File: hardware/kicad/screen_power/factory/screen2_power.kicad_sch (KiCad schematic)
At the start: 18 parts, among them J203 SCREEN POWER 5V 3A, Q201 2N7002, Q202 2N7002, U202 SN74LVC1G14DBVR, U203 TPS25221DBVR, U204 TPS25810RVCR

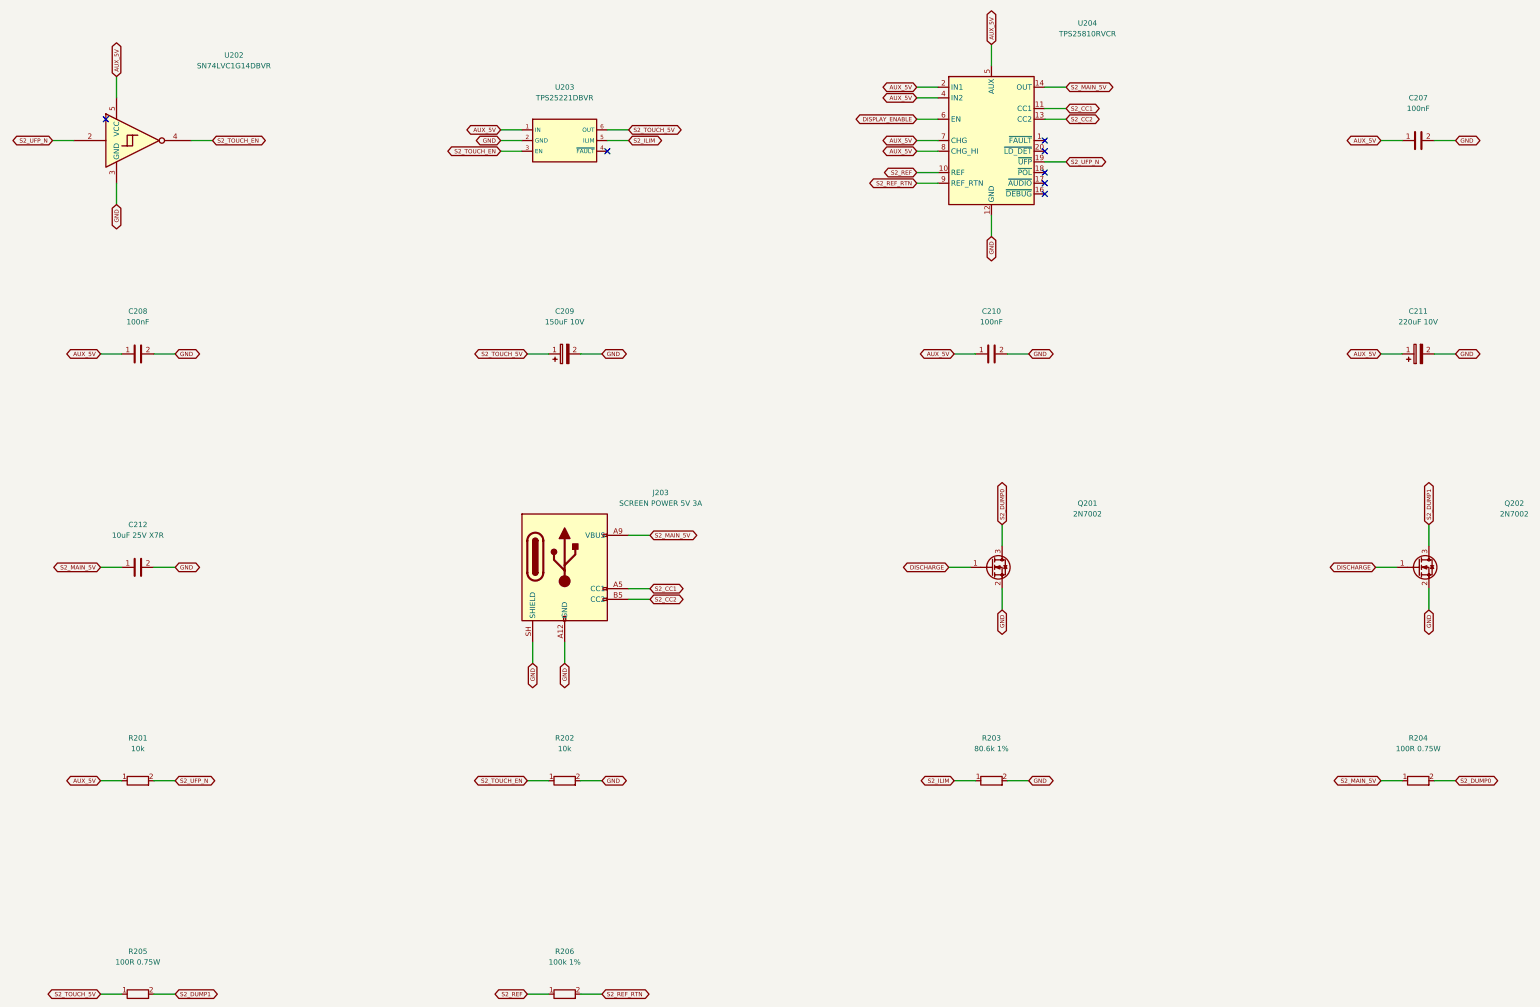
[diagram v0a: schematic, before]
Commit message: refactor(hardware): simplify and compact screen power boards
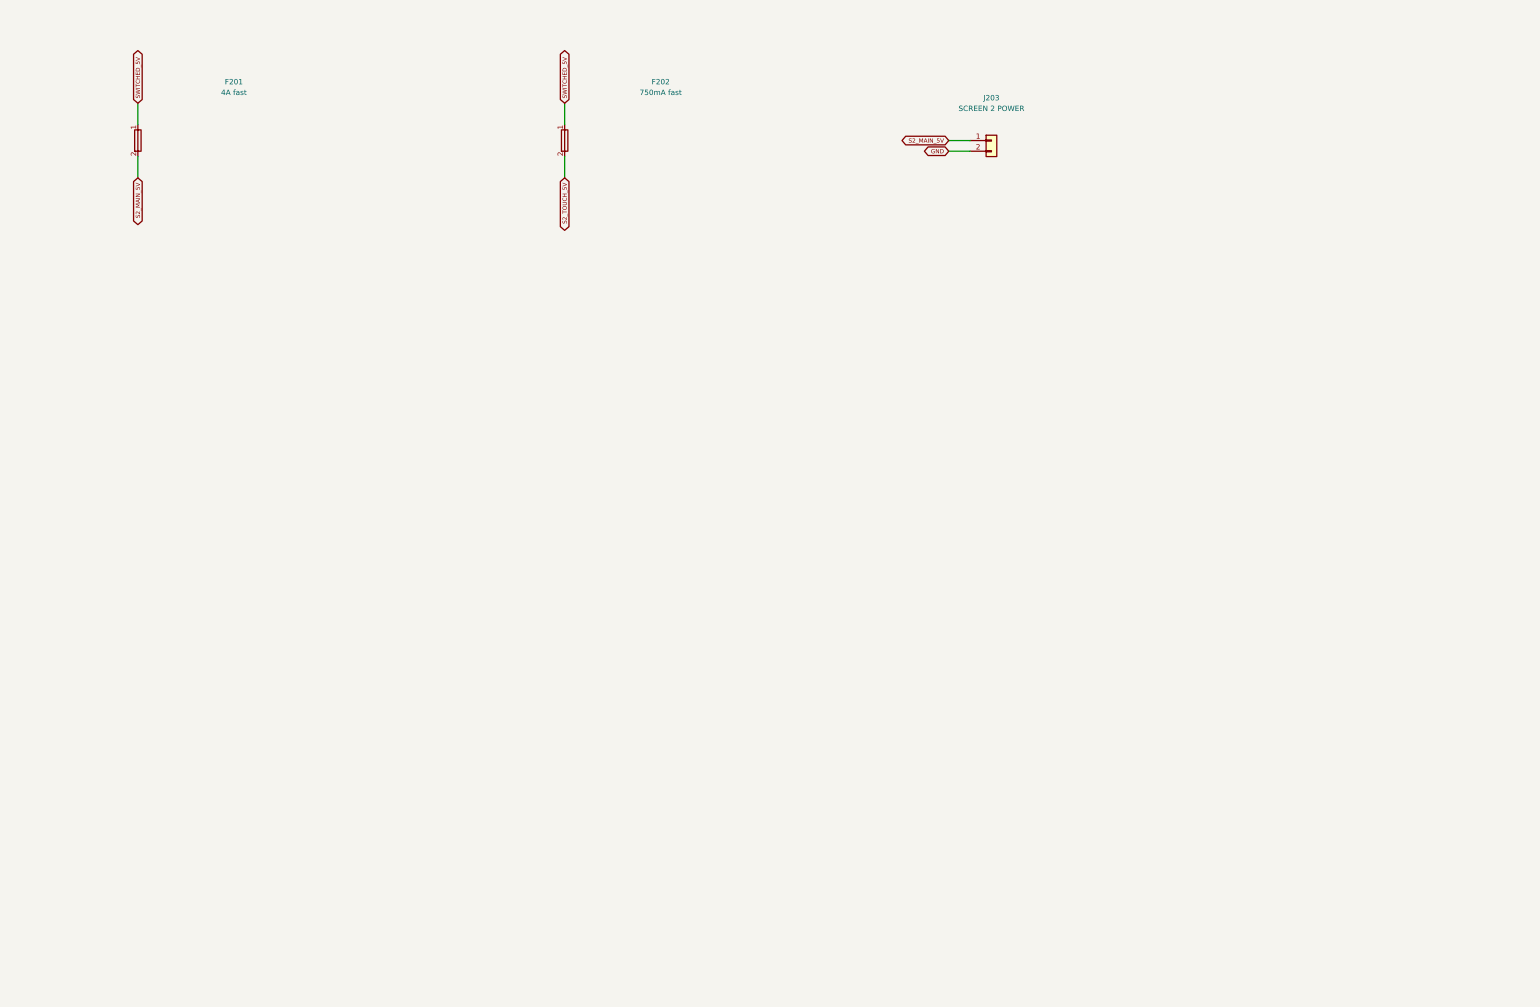
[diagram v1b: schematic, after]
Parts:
- removed C207, C208, C210: 100nF, Capacitor_SMD:C_0805_2012Metric, symbol screen_symbols:Device_C
- removed C209: 150uF 10V, Capacitor_THT:CP_Radial_D5.0mm_P2.00mm, symbol screen_symbols:Device_C_Polarized
- removed C211: 220uF 10V, Capacitor_THT:CP_Radial_D6.3mm_P2.50mm, symbol screen_symbols:Device_C_Polarized
- removed C212: 10uF 25V X7R, Capacitor_SMD:C_1210_3225Metric, symbol screen_symbols:Device_C
- removed Q201, Q202: 2N7002, Package_TO_SOT_SMD:SOT-23, symbol screen_symbols:Transistor_FET_2N7002
- removed R201, R202: 10k, Resistor_SMD:R_0805_2012Metric, symbol screen_symbols:Device_R
- removed R203: 80.6k 1%, Resistor_SMD:R_0805_2012Metric, symbol screen_symbols:Device_R
- removed R204, R205: 100R 0.75W, Resistor_SMD:R_2010_5025Metric, symbol screen_symbols:Device_R
- removed R206: 100k 1%, Resistor_SMD:R_0805_2012Metric, symbol screen_symbols:Device_R
- removed U202: SN74LVC1G14DBVR, Package_TO_SOT_SMD:SOT-23-5, symbol screen_symbols:74xGxx_SN74LVC1G14DBV
- removed U203: TPS25221DBVR, Package_TO_SOT_SMD:SOT-23-6, symbol screen_symbols:screen_power_TPS25221DBVR
- removed U204: TPS25810RVCR, Package_DFN_QFN:Texas_RVC0020A_WQFN-20-1EP_3x4mm_P0.5mm_EP1.6x2.6mm_ThermalVias, symbol screen_symbols:Interface_USB_TPS25810RVC
- added F201: 4A fast, screen_power:Fuse_Littelfuse_251_P12.70mm, symbol screen_symbols:Device_Fuse
- added F202: 750mA fast, screen_power:Fuse_Littelfuse_251_P12.70mm, symbol screen_symbols:Device_Fuse
- J203: value SCREEN POWER 5V 3A -> SCREEN 2 POWER; footprint Connector_USB:USB_C_Receptacle_GCT_USB4125-xx-x_6P_TopMnt_Horizontal -> Connector_JST:JST_VH_B2P-VH_1x02_P3.96mm_Vertical; symbol screen_symbols:Connector_USB_C_Receptacle_PowerOnly_6P -> screen_symbols:Connector_Generic_Conn_01x02; MPN USB4125-GF-A -> B2P-VH(LF)(SN)
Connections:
- net GND: now also J203.2 (Pin_2); no longer J203.A12 (GND), J203.B12 (GND), J203.SH (SHIELD)
- net S2_MAIN_5V: now also J203.1 (Pin_1), F201.2; no longer J203.A9 (VBUS), J203.B9 (VBUS)
- net S2_TOUCH_5V: now also F202.2
- removed net S2_CC1: J203.A5 (CC1)
- removed net S2_CC2: J203.B5 (CC2)
- new net SWITCHED_5V: F201.1, F202.1
- no-connect marks 7 -> 0
